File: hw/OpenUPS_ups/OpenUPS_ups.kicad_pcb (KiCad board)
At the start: 4 copper layers, 90 x 62 mm, 284 parts, among them J1001 USB4105-GF-A, J101 Barrel Jack, J102 XT30PW-M, J103 XT30PW-M, J104 S2B-PH-K_1x02, J105 S2B-PH-K_1x02, J106 Screw Terminal, J107 Screw Terminal, J108 Screw Terminal, J109 JST XH, J110 JST XH, J501 Conn_01x03, J701 0022053031, J702 0022053031, J901 Qwiic, J902 Qwiic, Q1001 2N7002, Q301 AON7534, Q302 AON7534, Q303 AON7534, Q304 AON7534, Q401 2N7002, Q402 AON7534, Q403 AON7534, Q404 AON7534, Q405 AON7534, Q406 AON7423, Q601 AON7534, Q602 AON7534, Q603 AON7534, Q604 AON7534, Q701 2N7002, Q702 2N7002, U1001 MCP6547, U1002 AP22814BW5, U1003 NUP2301MW6T1G, U101 AVR32DB48x-xPT, U102 NUP2301MW6T1G, U103 LM75BTP,147, U201 TPS51397A, U202 INA180A3, U301 NCP81599, U401 NCP431, U402 BD99950, U403 MCP6001R, U404 DZDH0401DW, U405 INA180A1, U601 NCP81599, U701 NUP2301MW6T1G, U702 NUP2301MW6T1G, U801 AP7383-33W5, U901 π220N31

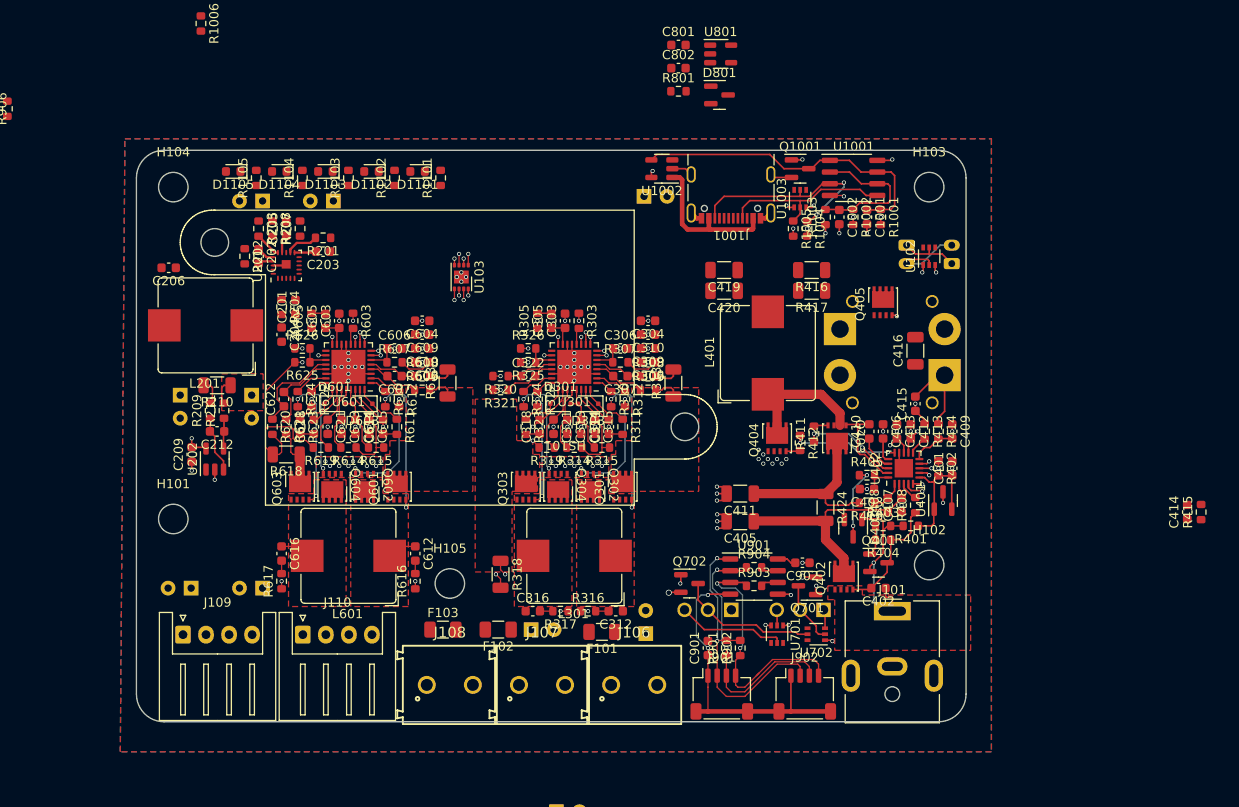
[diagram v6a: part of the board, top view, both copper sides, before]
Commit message: PCB enlarged; 4 holes, LEDs and USB moved; two keepouts;
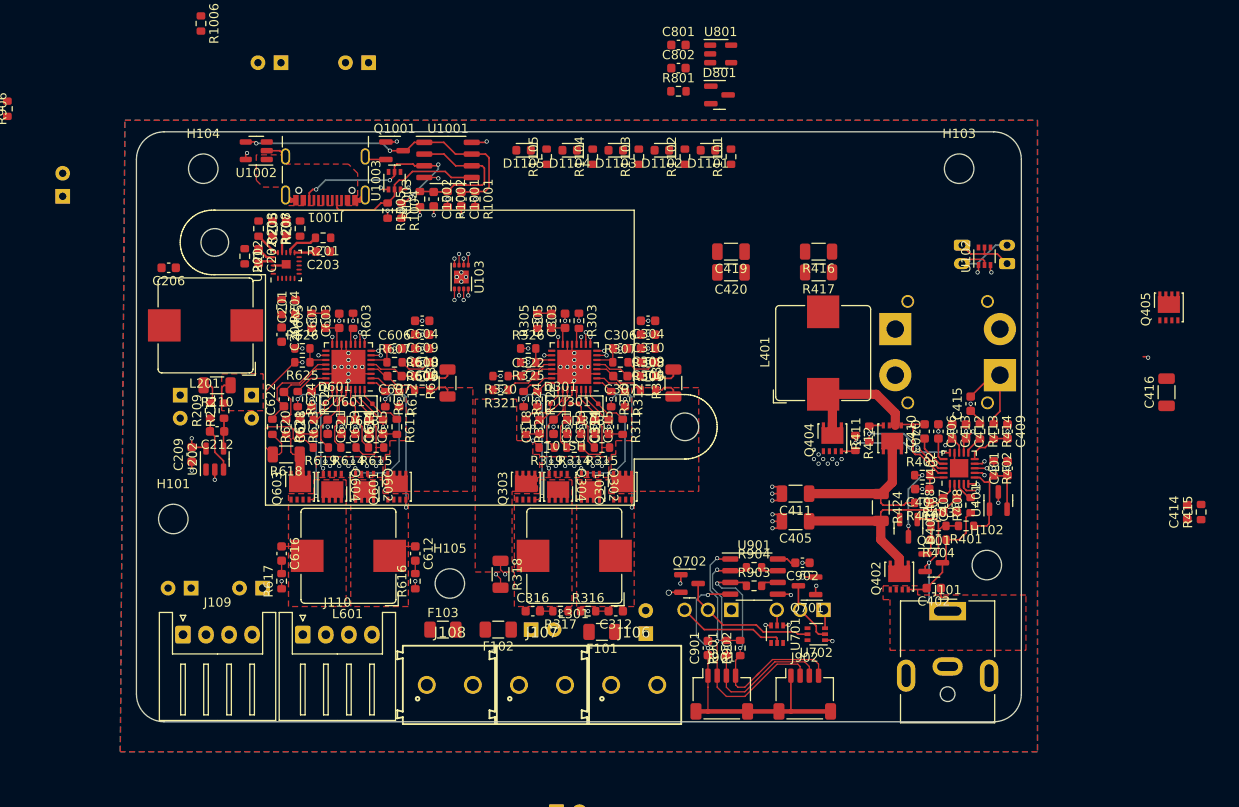
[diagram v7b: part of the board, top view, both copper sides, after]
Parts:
- moved C210 63.1 mm to (75.0, 77.0), turned to 90 degrees
- moved U1001 44.0 mm to (116.8, 73.0)
- moved C1001 44.0 mm to (118.2, 77.3)
- moved C1002 44.0 mm to (115.2, 77.3)
- moved J1001 44.0 mm to (103.5, 73.8)
- moved Q1001 44.0 mm to (111.0, 72.0)
- moved R1001 44.0 mm to (119.8, 77.3)
- moved R1002 44.0 mm to (116.8, 77.3)
- moved R1003 44.0 mm to (113.8, 77.3)
- moved R1004 44.0 mm to (111.8, 78.5)
- moved R1005 44.0 mm to (110.2, 78.5)
- moved U1002 44.0 mm to (96.0, 72.0)
- moved U1003 44.0 mm to (111.0, 75.3)
- moved D1101 31.6 mm to (145.0, 72.0)
- moved D1102 31.6 mm to (140.0, 72.0)
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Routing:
- net Net-(U1002-OUT): track 16.3 -> 0.00 mm
- net Net-(J1001-CC1): track 19.4 -> 18.3 mm
- net Net-(Q1001-D): track 34.8 -> 34.3 mm, vias 0 -> 2
- net Net-(J1001-CC2): track 23.1 -> 22.8 mm, vias 2 -> 4
- added copper zone on F.Cu, net Net-(U1002-OUT)
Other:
- board size 90 x 62 mm -> 96 x 64 mm

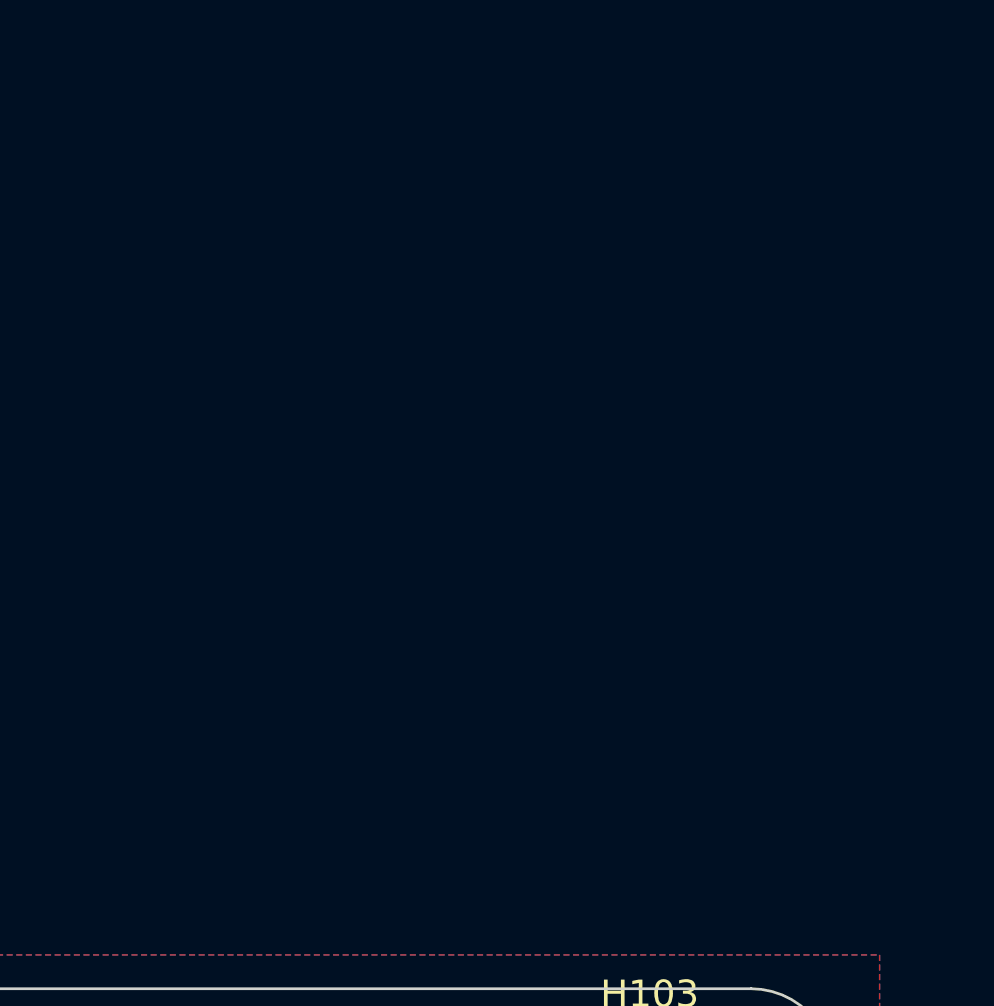
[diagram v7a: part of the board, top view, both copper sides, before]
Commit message: Preliminary BMS circuit (not done yet)
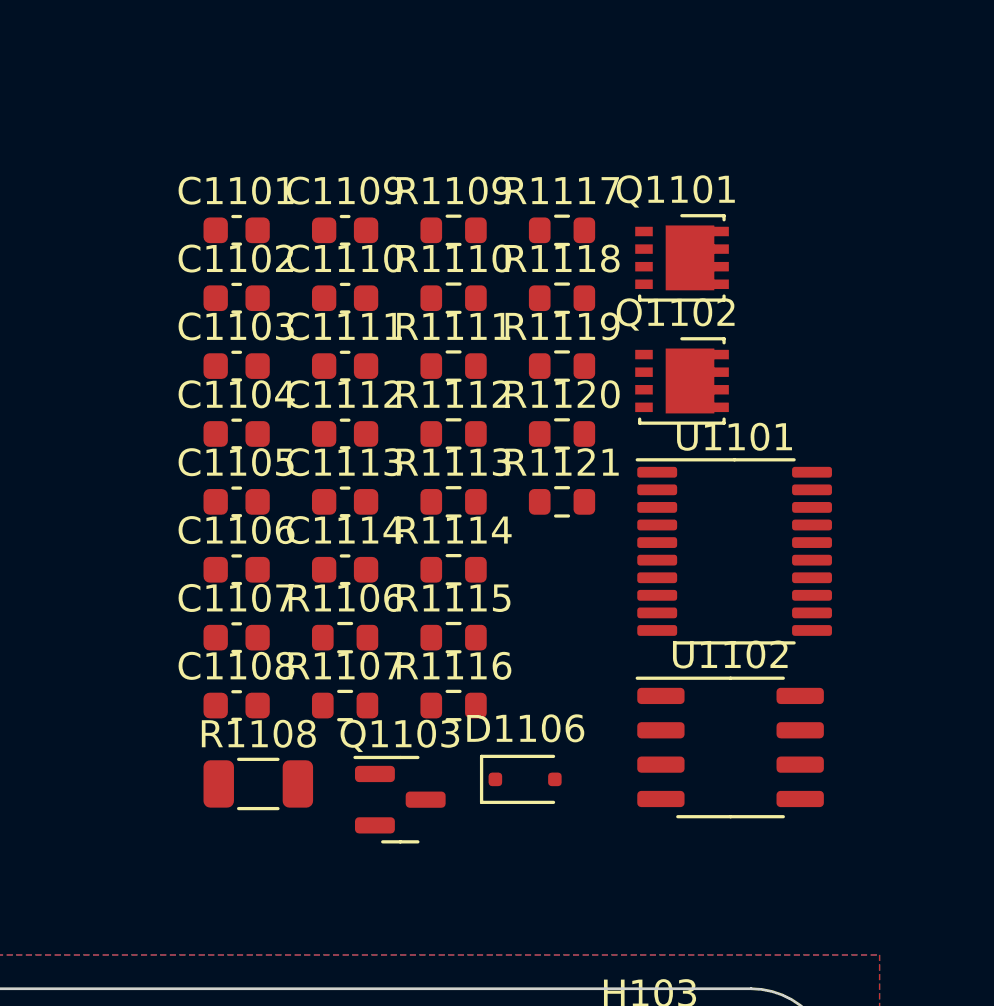
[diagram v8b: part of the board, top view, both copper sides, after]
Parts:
- added C1101: 100n, Capacitor_SMD:C_0603_1608Metric, F.Cu at (157.0, 42.0)
- added C1102: 100n, Capacitor_SMD:C_0603_1608Metric, F.Cu at (157.0, 44.5)
- added C1103: 4u7 6.3V, Capacitor_SMD:C_0603_1608Metric, F.Cu at (157.0, 47.0)
- added C1104: 1u 16V, Capacitor_SMD:C_0603_1608Metric, F.Cu at (157.0, 49.5)
- added C1105: Cf, Capacitor_SMD:C_0603_1608Metric, F.Cu at (157.0, 52.0)
- added C1106: Cc, Capacitor_SMD:C_0603_1608Metric, F.Cu at (157.0, 54.5)
- added C1107: 0R, Capacitor_SMD:C_0603_1608Metric, F.Cu at (157.0, 57.0)
- added C1108: Cc, Capacitor_SMD:C_0603_1608Metric, F.Cu at (157.0, 59.5)
- added C1109: Cc, Capacitor_SMD:C_0603_1608Metric, F.Cu at (161.0, 42.0)
- added C1110: Cc, Capacitor_SMD:C_0603_1608Metric, F.Cu at (161.0, 44.5)
- added C1111: 100n, Capacitor_SMD:C_0603_1608Metric, F.Cu at (161.0, 47.0)
- added C1112: 100n, Capacitor_SMD:C_0603_1608Metric, F.Cu at (161.0, 49.5)
- added C1113: 100n, Capacitor_SMD:C_0603_1608Metric, F.Cu at (161.0, 52.0)
- added C1114: 1u 16V, Capacitor_SMD:C_0603_1608Metric, F.Cu at (161.0, 54.5)
- added D1106: BAT54J, Diode_SMD:D_SOD-323F, F.Cu at (167.6, 62.3)
- added Q1101: AON7534, footprints:DFN 3x3 MOSFET, F.Cu at (173.4, 43.0)
- added Q1102: AON7534, footprints:DFN 3x3 MOSFET, F.Cu at (173.4, 47.5)
- added Q1103: BSS84, Package_TO_SOT_SMD:SOT-23, F.Cu at (163.0, 63.0)
- added R1106: 3k3, Resistor_SMD:R_0603_1608Metric, F.Cu at (161.0, 57.0)
- added R1107: 3k3, Resistor_SMD:R_0603_1608Metric, F.Cu at (161.0, 59.5)
- added R1108: Rsns, Resistor_SMD:R_1206_3216Metric, F.Cu at (157.8, 62.4)
- added R1109: Rf, Resistor_SMD:R_0603_1608Metric, F.Cu at (165.0, 42.0)
- added R1110: NM, Resistor_SMD:R_0603_1608Metric, F.Cu at (165.0, 44.5)
- added R1111: NM, Resistor_SMD:R_0603_1608Metric, F.Cu at (165.0, 47.0)
- added R1112: Rc, Resistor_SMD:R_0603_1608Metric, F.Cu at (165.0, 49.5)
- added R1113: NM, Resistor_SMD:R_0603_1608Metric, F.Cu at (165.0, 52.0)
- added R1114: Rc, Resistor_SMD:R_0603_1608Metric, F.Cu at (165.0, 54.5)
- added R1115: Rc, Resistor_SMD:R_0603_1608Metric, F.Cu at (165.0, 57.0)
- added R1116: Rc, Resistor_SMD:R_0603_1608Metric, F.Cu at (165.0, 59.5)
- added R1117: 100, Resistor_SMD:R_0603_1608Metric, F.Cu at (169.0, 42.0)
- added R1118: 100, Resistor_SMD:R_0603_1608Metric, F.Cu at (169.0, 44.5)
- added R1119: 1M, Resistor_SMD:R_0603_1608Metric, F.Cu at (169.0, 47.0)
- added R1120: 1M, Resistor_SMD:R_0603_1608Metric, F.Cu at (169.0, 49.5)
- added R1121: 1M, Resistor_SMD:R_0603_1608Metric, F.Cu at (169.0, 52.0)
- added U1101: BQ76920PW, Package_SO:TSSOP-20_4.4x6.5mm_P0.65mm, F.Cu at (175.4, 53.8)
- added U1102: π220N31, Package_SO:SO-8_3.9x4.9mm_P1.27mm, F.Cu at (175.2, 61.1)
